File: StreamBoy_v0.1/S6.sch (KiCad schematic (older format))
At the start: 1 part, among them U1 XC6SLX9-TQG144

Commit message: Bunch of stuff
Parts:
- added C? (x6): 0.47uF, Capacitor_SMD:C_0805_2012Metric, symbol Device:C
- added C? (x10): 4.7uF, Capacitor_SMD:C_0805_2012Metric, symbol Device:C
- added C? (x4): 100uF, Capacitor_SMD:C_0805_2012Metric, symbol Device:C
- added R? (x10): R, Resistor_SMD:R_0805_2012Metric, symbol Device:R
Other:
- moved on the sheet: U1D

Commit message: Power to the masses
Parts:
- removed C? (x3): 0.47uF, Capacitor_SMD:C_0805_2012Metric, symbol Device:C
- removed C? (x8): 4.7uF, Capacitor_SMD:C_0805_2012Metric, symbol Device:C
- removed C? (x3): 100uF, Capacitor_SMD:C_0805_2012Metric, symbol Device:C
- removed R? (x2): R, Resistor_SMD:R_0805_2012Metric, symbol Device:R
- added C? (x3): 0.47uF, Capacitor_SMD:C_0805_2012Metric, symbol Device:C
- added C? (x8): 4.7uF, Capacitor_SMD:C_0805_2012Metric, symbol Device:C
- added C? (x3): 100uF, Capacitor_SMD:C_0805_2012Metric, symbol Device:C
- added R? (x2): 4.7KOhm, Resistor_SMD:R_0805_2012Metric, symbol Device:R
- R?: value R -> 4.7KOhm
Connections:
- net VCC3: now reaches U1.103 (VCCO_1)
- net VCC3: now also C?.1, C?.1, C?.1, C?.1, C?.1, R?.2, U1.122 (VCCO_0), U1.125 (VCCO_0), U1.129 (VCCAUX), U1.135 (VCCO_0), U1.18 (VCCO_3), U1.20 (VCCAUX), U1.31 (VCCO_3), U1.36 (VCCAUX), U1.4 (VCCO_3), U1.42 (VCCO_2), U1.53 (VCCAUX), U1.63 (VCCO_2), U1.76 (VCCO_1), U1.86 (VCCO_1), U1.90 (VCCAUX), C?.1, C?.1, C?.1, C?.1, C?.1, C?.1, C?.1, C?.1, C?.1, R?.1, R?.1
- net GND: now reaches C?.2
- net GND: now also C?.2, C?.2, C?.2, C?.2, C?.2, U1.108 (GND), U1.113 (GND), U1.13 (GND), U1.130 (GND), U1.136 (GND), U1.25 (GND), U1.3 (GND), U1.49 (GND), U1.54 (GND), U1.68 (GND), U1.77 (GND), U1.91 (GND), U1.96 (GND), C?.2, C?.2, C?.2, C?.2, C?.2, C?.2, C?.2, C?.2, C?.2, C?.2, C?.2, C?.2, C?.2, C?.2
- net VCC1V2: now reaches C?.1
- net VCC1V2: now also U1.128 (VCCINT), U1.19 (VCCINT), U1.28 (VCCINT), U1.52 (VCCINT), U1.89 (VCCINT), C?.1, C?.1, C?.1, C?.1, C?.1
- net at R?.1: now also U1.71 (DONE_2)
- net at U1.37 (PROGRAM_B_2): now also R?.2
- net at U1.72 (CMPCS_B_2): now also R?.2
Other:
- moved on the sheet: C?, R?, U1A, U1B, U1C, U1D

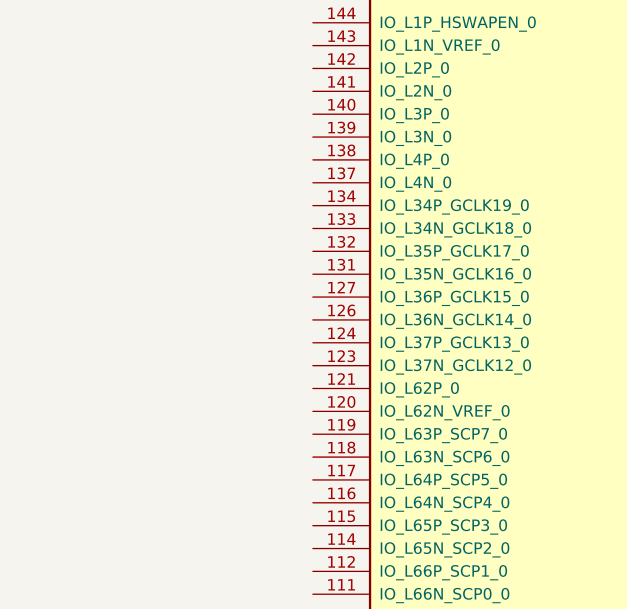
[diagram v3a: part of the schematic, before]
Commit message: Add esp pins to fpga
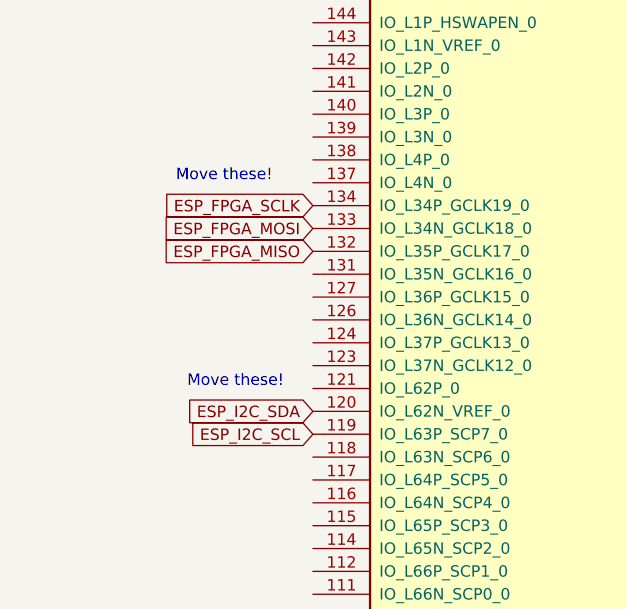
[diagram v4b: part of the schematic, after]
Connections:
- net ESP_I2C_SCL: now reaches U1.119 (IO_L63P_SCP7_0)
- net ESP_I2C_SDA: now reaches U1.120 (IO_L62N_VREF_0)
- net ESP_FPGA_MISO: now reaches U1.132 (IO_L35P_GCLK17_0)
- net ESP_FPGA_MOSI: now reaches U1.133 (IO_L34N_GCLK18_0)
- net ESP_FPGA_SCLK: now reaches U1.134 (IO_L34P_GCLK19_0)
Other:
- note added: "Move these!"
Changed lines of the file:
@@
 EESchema Schematic File Version 4
-EELAYER 30 0
+LIBS:StreamBoy-cache
+EELAYER 29 0
 EELAYER END
 $Descr A3 16535 11693
@@
 Text GLabel 5500 8600 2    50   Input ~ 0
 VCC3
+Text GLabel 2450 3550 0    50   Input ~ 0
+ESP_I2C_SDA
+Text GLabel 2450 3650 0    50   Input ~ 0
+ESP_I2C_SCL
+Text GLabel 2450 2650 0    50   Input ~ 0
+ESP_FPGA_SCLK
+Text GLabel 2450 2750 0    50   Input ~ 0
+ESP_FPGA_MOSI
+Text GLabel 2450 2850 0    50   Input ~ 0
+ESP_FPGA_MISO
+Text Notes 1850 2550 0    50   ~ 0
+Move these!
+Text Notes 1900 3450 0    50   ~ 0
+Move these!
 $EndSCHEMATC

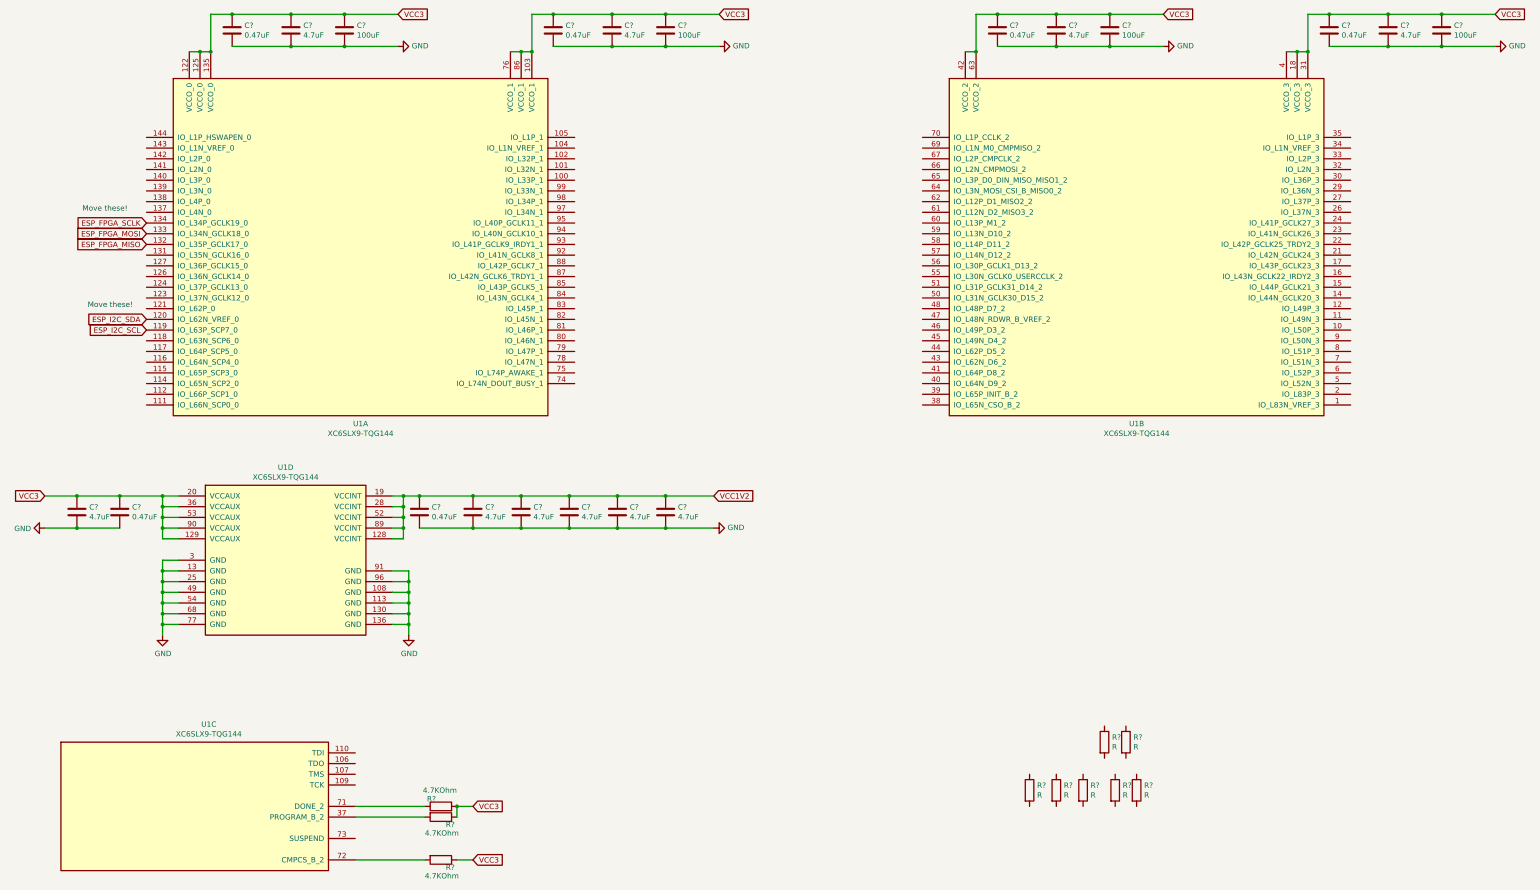
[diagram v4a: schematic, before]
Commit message: Connect RAM temporarily
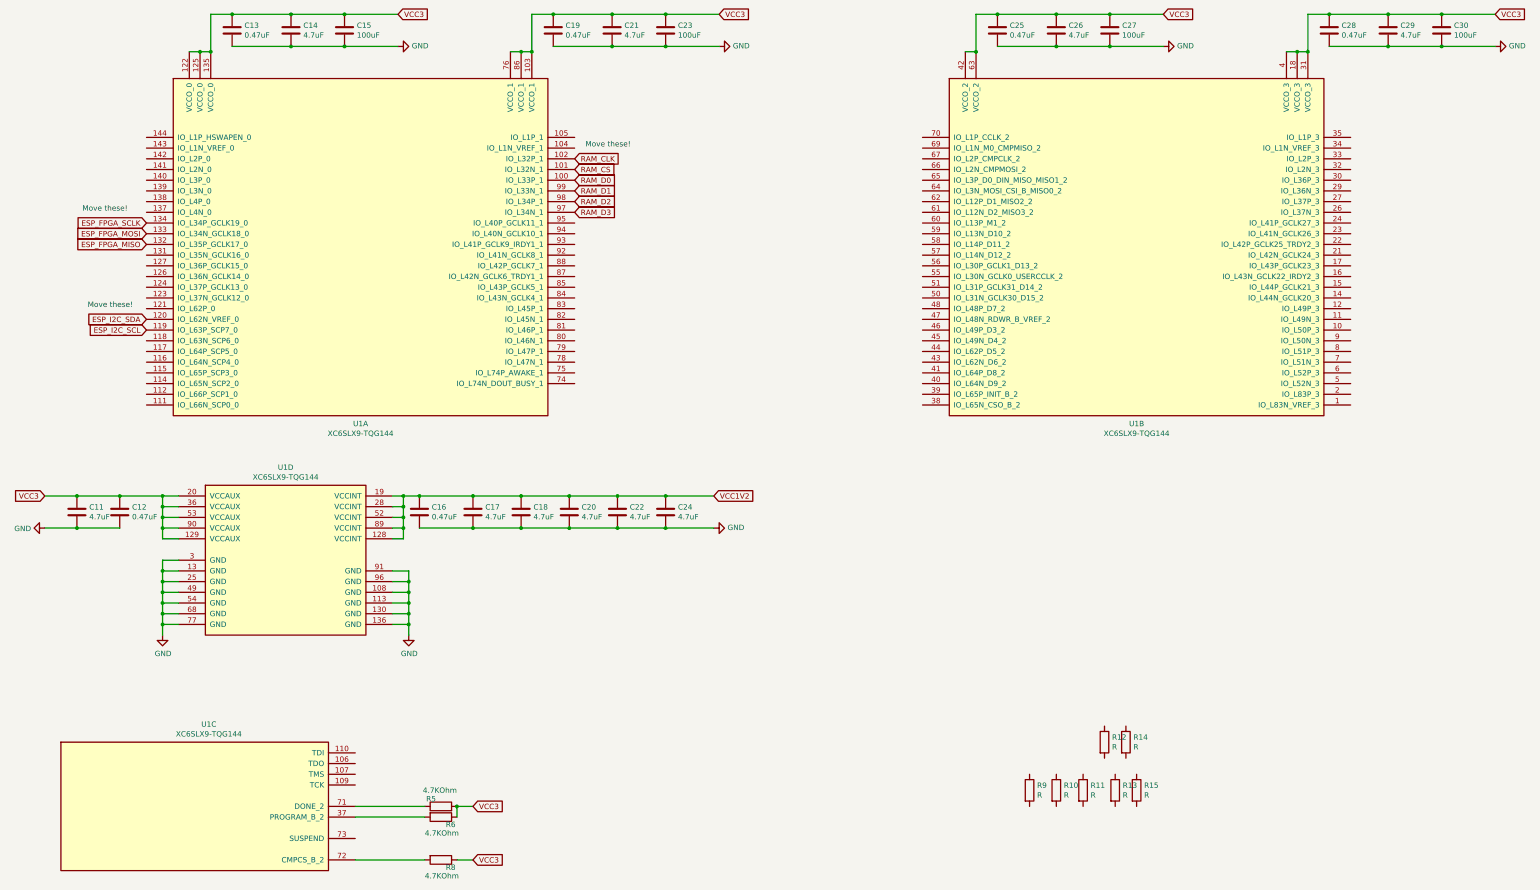
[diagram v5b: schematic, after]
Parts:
- gave numbers to parts that had none: 30
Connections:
- net RAM_D0: now reaches U1.100 (IO_L33P_1)
- net RAM_CS: now reaches U1.101 (IO_L32N_1)
- net RAM_CLK: now reaches U1.102 (IO_L32P_1)
- net RAM_D3: now reaches U1.97 (IO_L34N_1)
- net RAM_D2: now reaches U1.98 (IO_L34P_1)
- net RAM_D1: now reaches U1.99 (IO_L33N_1)

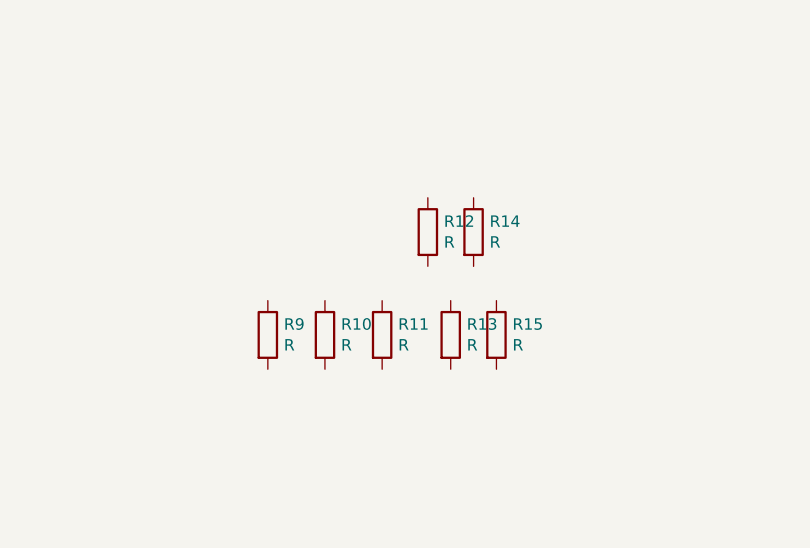
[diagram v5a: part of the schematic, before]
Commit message: Update some labels
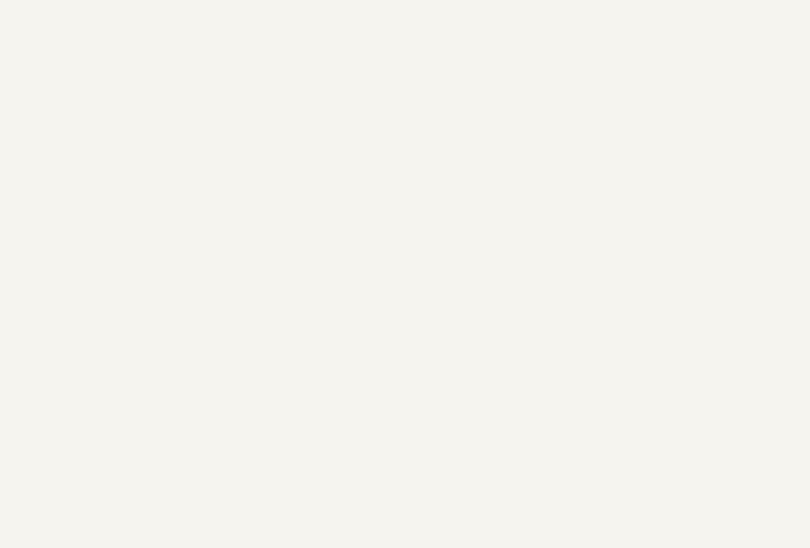
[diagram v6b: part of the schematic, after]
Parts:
- removed R10, R11, R12, R13, R14, R15, R9: R, Resistor_SMD:R_0805_2012Metric, symbol Device:R
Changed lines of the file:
@@
-$EndComp
-$Comp
-L Device:R R?
-U 1 1 5E0E10F9
-P 11600 7500
-AR Path="/5E0FF68C/5E0E10F9" Ref="R?"  Part="1"
-AR Path="/5E0E69A0/5E0E10F9" Ref="R14"  Part="1"
-F 0 "R14" H 11670 7546 50  0000 L CNN
-F 1 "R" H 11670 7455 50  0000 L CNN
-F 2 "Resistor_SMD:R_0805_2012Metric" V 11530 7500 50  0001 C CNN
-F 3 "~" H 11600 7500 50  0001 C CNN
-	1    11600 7500
-	1    0    0    -1
 $EndComp
 $Comp
@@
 	0    -1   -1   0
 $EndComp
-$Comp
-L Device:R R?
-U 1 1 5E0F11BE
-P 11400 7500
-AR Path="/5E0FF68C/5E0F11BE" Ref="R?"  Part="1"
-AR Path="/5E0E69A0/5E0F11BE" Ref="R12"  Part="1"
-F 0 "R12" H 11470 7546 50  0000 L CNN
-F 1 "R" H 11470 7455 50  0000 L CNN
-F 2 "Resistor_SMD:R_0805_2012Metric" V 11330 7500 50  0001 C CNN
-F 3 "~" H 11400 7500 50  0001 C CNN
-	1    11400 7500
-	1    0    0    -1
-$EndComp
-$Comp
-L Device:R R?
-U 1 1 5E0F2BA2
-P 10700 7950
-AR Path="/5E0FF68C/5E0F2BA2" Ref="R?"  Part="1"
-AR Path="/5E0E69A0/5E0F2BA2" Ref="R9"  Part="1"
-F 0 "R9" H 10770 7996 50  0000 L CNN
-F 1 "R" H 10770 7905 50  0000 L CNN
-F 2 "Resistor_SMD:R_0805_2012Metric" V 10630 7950 50  0001 C CNN
-F 3 "~" H 10700 7950 50  0001 C CNN
-	1    10700 7950
-	1    0    0    -1
-$EndComp
-$Comp
-L Device:R R?
-U 1 1 5E0F2D03
-P 10950 7950
-AR Path="/5E0FF68C/5E0F2D03" Ref="R?"  Part="1"
-AR Path="/5E0E69A0/5E0F2D03" Ref="R10"  Part="1"
-F 0 "R10" H 11020 7996 50  0000 L CNN
-F 1 "R" H 11020 7905 50  0000 L CNN
-F 2 "Resistor_SMD:R_0805_2012Metric" V 10880 7950 50  0001 C CNN
-F 3 "~" H 10950 7950 50  0001 C CNN
-	1    10950 7950
-	1    0    0    -1
-$EndComp
-$Comp
-L Device:R R?
-U 1 1 5E0F2DE1
-P 11200 7950
-AR Path="/5E0FF68C/5E0F2DE1" Ref="R?"  Part="1"
-AR Path="/5E0E69A0/5E0F2DE1" Ref="R11"  Part="1"
-F 0 "R11" H 11270 7996 50  0000 L CNN
-F 1 "R" H 11270 7905 50  0000 L CNN
-F 2 "Resistor_SMD:R_0805_2012Metric" V 11130 7950 50  0001 C CNN
-F 3 "~" H 11200 7950 50  0001 C CNN
-	1    11200 7950
-	1    0    0    -1
-$EndComp
-$Comp
-L Device:R R?
-U 1 1 5E0F3BDF
-P 11700 7950
-AR Path="/5E0FF68C/5E0F3BDF" Ref="R?"  Part="1"
-AR Path="/5E0E69A0/5E0F3BDF" Ref="R15"  Part="1"
-F 0 "R15" H 11770 7996 50  0000 L CNN
-F 1 "R" H 11770 7905 50  0000 L CNN
-F 2 "Resistor_SMD:R_0805_2012Metric" V 11630 7950 50  0001 C CNN
-F 3 "~" H 11700 7950 50  0001 C CNN
-	1    11700 7950
-	1    0    0    -1
-$EndComp
-$Comp
-L Device:R R?
-U 1 1 5E0F3BE5
-P 11500 7950
-AR Path="/5E0FF68C/5E0F3BE5" Ref="R?"  Part="1"
-AR Path="/5E0E69A0/5E0F3BE5" Ref="R13"  Part="1"
-F 0 "R13" H 11570 7996 50  0000 L CNN
-F 1 "R" H 11570 7905 50  0000 L CNN
-F 2 "Resistor_SMD:R_0805_2012Metric" V 11430 7950 50  0001 C CNN
-F 3 "~" H 11500 7950 50  0001 C CNN
-	1    11500 7950
-	1    0    0    -1
-$EndComp
 Wire Wire Line

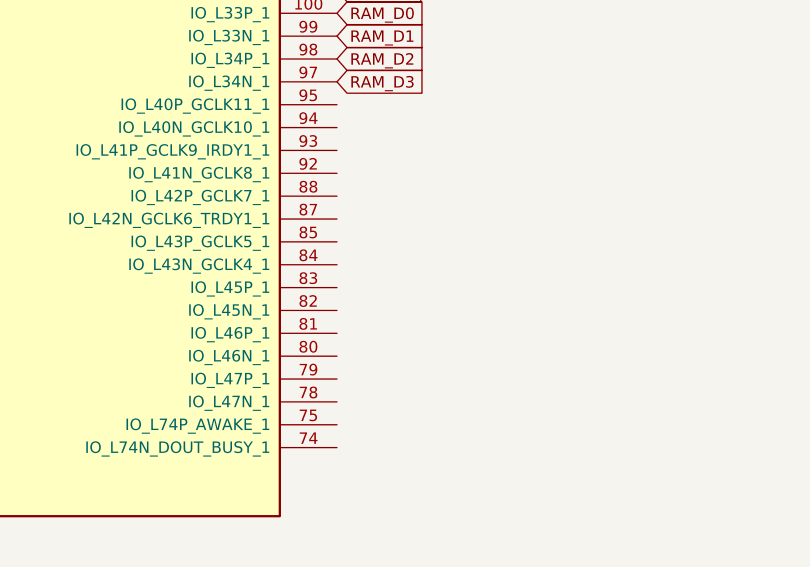
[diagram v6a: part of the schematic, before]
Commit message: Add leds and buttons to debug
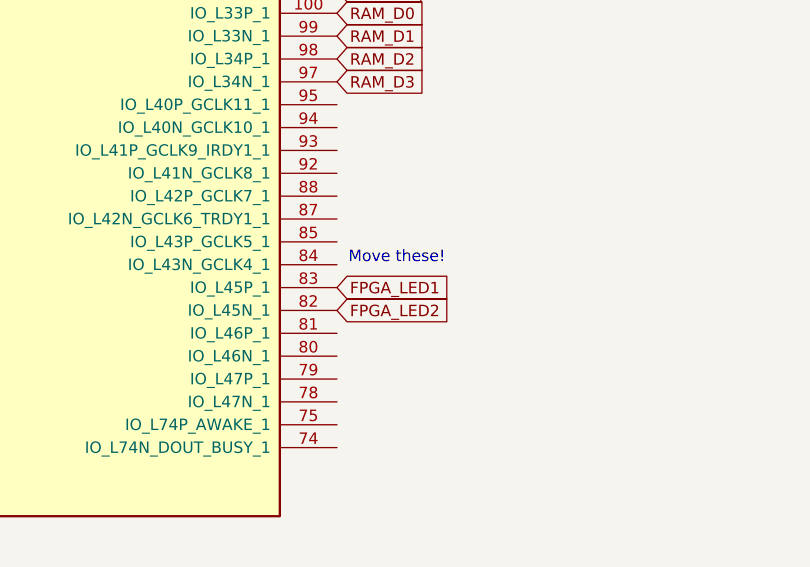
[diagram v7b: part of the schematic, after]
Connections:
- net FPGA_LED2: now reaches U1.82 (IO_L45N_1)
- net FPGA_LED1: now reaches U1.83 (IO_L45P_1)
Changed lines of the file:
@@
 Text Notes 6550 1950 0    50   ~ 0
 Move these!
+Text GLabel 6450 3450 2    50   Input ~ 0
+FPGA_LED1
+Text GLabel 6450 3550 2    50   Input ~ 0
+FPGA_LED2
+Text Notes 6500 3350 0    50   ~ 0
+Move these!
 $EndSCHEMATC
